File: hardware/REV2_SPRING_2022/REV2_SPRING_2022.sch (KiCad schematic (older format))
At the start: 38 parts, among them J101 Screw_Terminal_01x02, J102 Screw_Terminal_01x02, J103 Conn_01x02_Female, J104 Screw_Terminal_01x02, J105 Conn_01x02_Female, J107 Screw_Terminal_01x02, J109 Conn_01x02_Female, J110 Conn_01x02_Female, Q101 Q_NMOS_GDS, Q102 Q_NMOS_GDS, U1 Teensy3.6_All_Pins, U2 PA16165_Breakout, U3 MPL3115A2_Breakout, U4 BNO055_Breakout, U5 RFM69HCW_Breakout

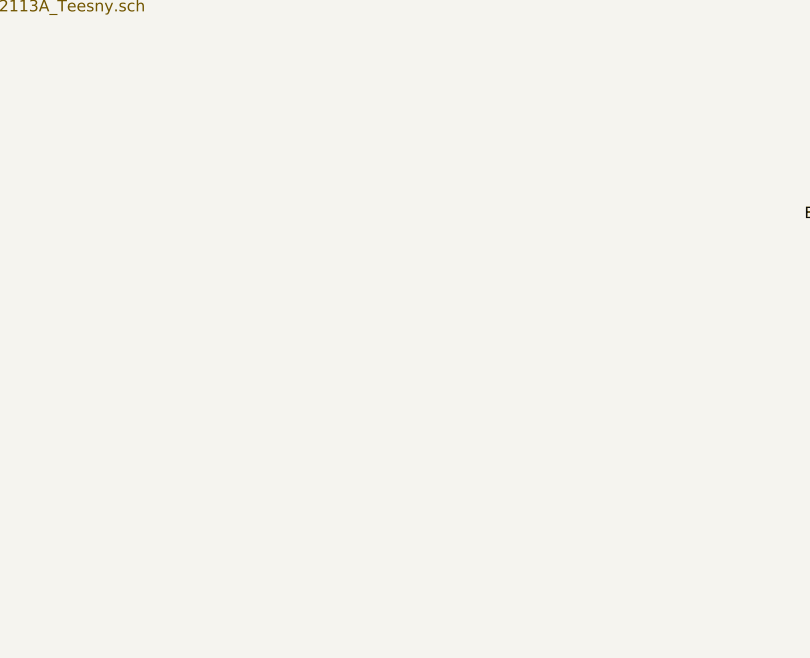
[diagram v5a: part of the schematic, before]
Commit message: add pullup resistors on TPS stat pins
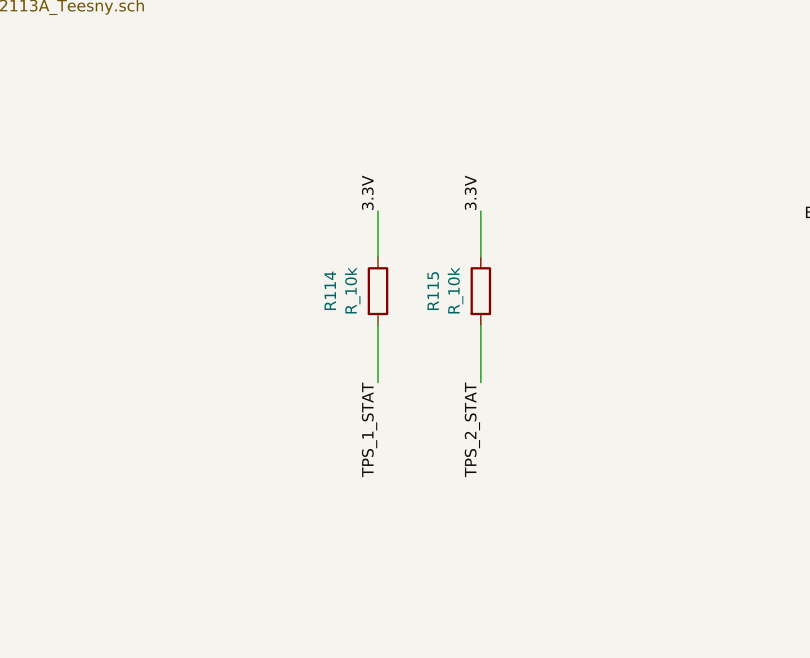
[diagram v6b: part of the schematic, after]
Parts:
- added R114, R115: R_10k, Resistor_SMD:R_0805_2012Metric_Pad1.20x1.40mm_HandSolder, symbol Device:R
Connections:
- net 3.3V: now also R114.1, R115.1
- net TPS_1_STAT: now also R114.2
- net TPS_2_STAT: now also R115.2
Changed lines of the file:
@@
 	0    1    -1   0
 $EndComp
+Text Label 16700 6500 1    50   ~ 0
+3.3V
+$Comp
+L Device:R R114
+U 1 1 61F61A24
+P 16700 6850
+F 0 "R114" V 16493 6850 50  0000 C CNN
+F 1 "R_10k" V 16584 6850 50  0000 C CNN
+F 2 "Resistor_SMD:R_0805_2012Metric_Pad1.20x1.40mm_HandSolder" V 16630 6850 50  0001 C CNN
+F 3 "~" H 16700 6850 50  0001 C CNN
+	1    16700 6850
+	1    0    0    -1
+$EndComp
+Text Label 16700 7250 3    50   ~ 0
+TPS_1_STAT
+Wire Wire Line
+	16700 6500 16700 6700
+Wire Wire Line
+	16700 7000 16700 7250
+$Comp
+L Device:R R115
+U 1 1 61F6F212
+P 17150 6850
+F 0 "R115" V 16943 6850 50  0000 C CNN
+F 1 "R_10k" V 17034 6850 50  0000 C CNN
+F 2 "Resistor_SMD:R_0805_2012Metric_Pad1.20x1.40mm_HandSolder" V 17080 6850 50  0001 C CNN
+F 3 "~" H 17150 6850 50  0001 C CNN
+	1    17150 6850
+	1    0    0    -1
+$EndComp
+Text Label 17150 6500 1    50   ~ 0
+3.3V
+Text Label 17150 7250 3    50   ~ 0
+TPS_2_STAT
+Wire Wire Line
+	17150 6500 17150 6700
+Wire Wire Line
+	17150 7000 17150 7250
 $EndSCHEMATC
